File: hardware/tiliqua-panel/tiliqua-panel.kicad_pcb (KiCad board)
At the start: 2 copper layers, 30 x 128.5 mm, 13 parts

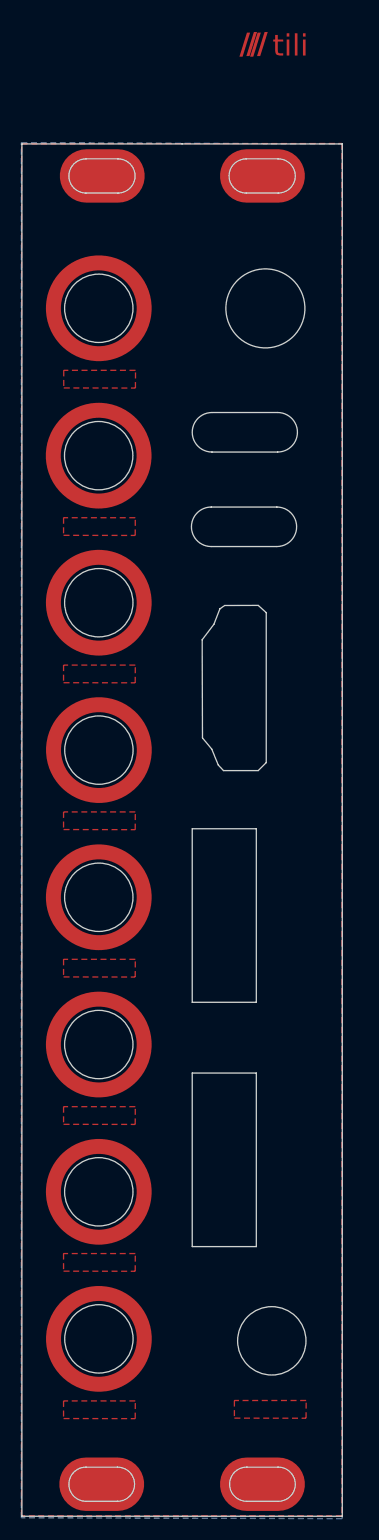
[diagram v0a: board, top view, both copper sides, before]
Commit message: fix panel slots and move some things
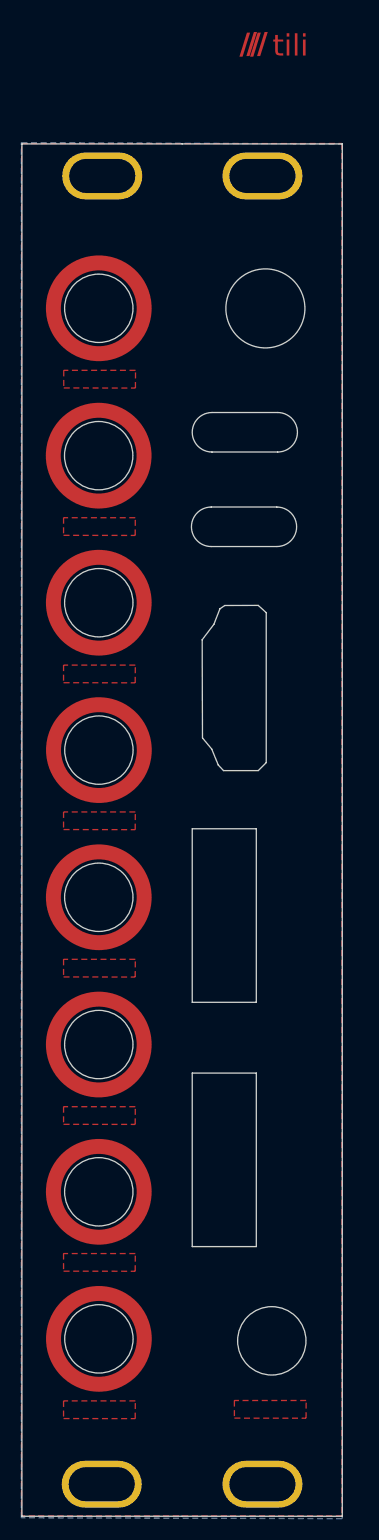
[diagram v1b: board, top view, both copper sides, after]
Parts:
- added E1: MountingHole_Pad, , F.Cu at (4.53, 3.00)
- added E2: MountingHole_Pad, , F.Cu at (19.5, 3.00)
- added E3: MountingHole_Pad, , F.Cu at (4.47, 125.5)
- added E4: MountingHole_Pad, , F.Cu at (19.5, 125.5)
- moved G*** 30.8 mm to (25.8, 72.0), turned to 0 degrees
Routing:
- added copper zone on B.Cu, net GND
- added copper zone on F.Cu, net GND
- removed copper zone on B.Cu, net (none)
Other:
- outline, holes or cut-outs redrawn
- board text added: "ctrl"
- board text added: "dbg"
- board text removed: "control"
- board text removed: "debug"

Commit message: more panel improvements
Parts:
- moved G*** 1.05 mm to (25.8, 73.1)
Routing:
- removed copper zone on F.Cu, net (none)
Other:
- board text added: "usb2"
- board text removed: "ctrl"
- board text removed: "usb"

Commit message: text top bottom looks good
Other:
- board text added: "[tiliqua]"
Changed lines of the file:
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@@
+	)
+	(gr_line
+		(start 17.4 7.5)
+		(end 25.9 7.5)
+		(stroke
+			(width 0.2)
+			(type default)
+		)
+		(layer "F.Mask")
 	)
 	(gr_line
@@
 		)
 		(fill solid)
+		(layer "F.Mask")
+	)
+	(gr_line
+		(start -1.8 7.5)
+		(end 6.9 7.5)
+		(stroke
+			(width 0.2)
+			(type default)
+		)
 		(layer "F.Mask")
 	)
@@
 				)
 			)
+		)
+	)
+	(gr_text "[tiliqua]"
+		(at 12.1 7.5 0)
+		(layer "F.Mask")
+		(effects
+			(font
+				(face "Space Grotesk")
+				(size 1.6 1.6)
+				(thickness 0.32)
+				(bold yes)
+			)
+		)
+		(render_cache "[tiliqua]" 0
+			(polygon
+				(pts
+					(xy 8.228849 8.715011) (xy 8.14766 8.702744) (xy 8.076276 8.662376) (xy 8.063936 8.650922) (xy 8.018215 8.583047)
+					(xy 8.000798 8.504978) (xy 8.000238 8.4864) (xy 8.000238 6.698933) (xy 8.01243 6.617819) (xy 8.052553 6.546681)
+					(xy 8.063936 6.534411) (xy 8.132091 6.48869) (xy 8.210267 6.471273) (xy 8.228849 6.470713) (xy 8.609477 6.470713)
+					(xy 8.609477 6.712611) (xy 8.333971 6.712611) (xy 8.27473 6.764073) (xy 8.27379 6.779826) (xy 8.27379 8.405898)
+					(xy 8.316634 8.471472) (xy 8.333971 8.473113) (xy 8.609477 8.473113) (xy 8.609477 8.715011)
+				)
+			)
+			(polygon
+				(pts
+					(xy 9.227705 8.164) (xy 9.145319 8.152713) (xy 9.071888 8.115313) (xy 9.049505 8.095612) (xy 9.003023 8.02702)
+					(xy 8.983168 7.947656) (xy 8.981508 7.913113) (xy 8.981508 7.285898) (xy 8.703657 7.285898) (xy 8.703657 7.052988)
+					(xy 8.981508 7.052988) (xy 8.981508 6.707921) (xy 9.263657 6.707921) (xy 9.263657 7.052988) (xy 9.568472 7.052988)
+					(xy 9.568472 7.285898) (xy 9.263657 7.285898) (xy 9.263657 7.863874) (xy 9.308449 7.929449) (xy 9.326574 7.93109)
+					(xy 9.541508 7.93109) (xy 9.541508 8.164)
+				)
+			)
+			(polygon
+				(pts
+					(xy 9.822876 8.164) (xy 9.822876 7.052988) (xy 10.105025 7.052988) (xy 10.105025 8.164)
+				)
+			)
+			(polygon
+				(pts
+					(xy 9.964341 6.922855) (xy 9.886031 6.907275) (xy 9.835381 6.873616) (xy 9.791331 6.804122) (xy 9.782624 6.743874)
+					(xy 9.799317 6.6632) (xy 9.835381 6.614132) (xy 9.906295 6.572693) (xy 9.964341 6.564502) (xy 10.04386 6.580205)
+					(xy 10.094083 6.614132) (xy 10.137153 6.683625) (xy 10.145667 6.743874) (xy 10.129345 6.824547)
+					(xy 10.094083 6.873616) (xy 10.023458 6.914729)
+				)
+			)
+			(polygon
+				(pts
+					(xy 10.418437 8.164) (xy 10.418437 6.596156) (xy 10.700587 6.596156) (xy 10.700587 8.164)
+				)
+			)
+			(polygon
+				(pts
+					(xy 11.013999 8.164) (xy 11.013999 7.052988) (xy 11.296148 7.052988) (xy 11.296148 8.164)
+				)
+			)
+			(polygon
+				(pts
+					(xy 11.155465 6.922855) (xy 11.077154 6.907275) (xy 11.026504 6.873616) (xy 10.982455 6.804122)
+					(xy 10.973748 6.743874) (xy 10.99044 6.6632) (xy 11.026504 6.614132) (xy 11.097419 6.572693) (xy 11.155465 6.564502)
+					(xy 11.234984 6.580205) (xy 11.285206 6.614132) (xy 11.328277 6.683625) (xy 11.33679 6.743874)
+					(xy 11.320469 6.824547) (xy 11.285206 6.873616) (xy 11.214582 6.914729)
+				)
+			)
+			(polygon
+				(pts
+					(xy 12.137555 7.025712) (xy 12.219423 7.041417) (xy 12.289142 7.072136) (xy 12.354779 7.122574)
+					(xy 12.404726 7.183379) (xy 12.40716 7.187419) (xy 12.447411 7.187419) (xy 12.447411 7.052988)
+					(xy 12.725262 7.052988) (xy 12.725262 8.611843) (xy 12.443113 8.611843) (xy 12.443113 8.036212)
+					(xy 12.402471 8.036212) (xy 12.352859 8.097671) (xy 12.3376 8.111634) (xy 12.270585 8.154125) (xy 12.226616 8.171815)
+					(xy 12.150412 8.189401) (xy 12.07027 8.195171) (xy 12.057795 8.195263) (xy 11.975722 8.188813)
+					(xy 11.897541 8.169464) (xy 11.823253 8.137217) (xy 11.808863 8.129219) (xy 11.741895 8.081951)
+					(xy 11.683627 8.022699) (xy 11.634061 7.951464) (xy 11.625192 7.935779) (xy 11.591756 7.859632)
+					(xy 11.569262 7.774954) (xy 11.558455 7.692522) (xy 11.556023 7.626274) (xy 11.556023 7.597356)
+					(xy 11.838172 7.597356) (xy 11.838172 7.619631) (xy 11.845065 7.704296) (xy 11.868894 7.78401)
+					(xy 11.914765 7.854242) (xy 11.925318 7.865046) (xy 11.990487 7.912882) (xy 12.065629 7.940861)
+					(xy 12.142596 7.949066) (xy 12.220853 7.940861) (xy 12.296445 7.912882) (xy 12.361047 7.865046)
+					(xy 12.410217 7.79814) (xy 12.437206 7.721447) (xy 12.447074 7.639503) (xy 12.447411 7.619631)
+					(xy 12.447411 7.597356) (xy 12.440487 7.512692) (xy 12.416551 7.432977) (xy 12.370475 7.362746)
+					(xy 12.359875 7.351941) (xy 12.294883 7.304106) (xy 12.219731 7.276126) (xy 12.142596 7.267921)
+					(xy 12.058386 7.277849) (xy 11.98415 7.307634) (xy 11.925318 7.351941) (xy 11.875703 7.418847)
+					(xy 11.84847 7.49554) (xy 11.838513 7.577484) (xy 11.838172 7.597356) (xy 11.556023 7.597356) (xy 11.556023 7.590713)
+					(xy 11.560346 7.503249) (xy 11.573315 7.422576) (xy 11.598241 7.339934) (xy 11.625192 7.281599)
+					(xy 11.667937 7.214602) (xy 11.723914 7.151618) (xy 11.788822 7.100694) (xy 11.810035 7.087768)
+					(xy 11.883766 7.05294) (xy 11.960855 7.031012) (xy 12.041303 7.021983) (xy 12.057795 7.021725)
+				)
+			)
+			(polygon
+				(pts
+					(xy 13.461899 8.181976) (xy 13.383733 8.176175) (xy 13.305068 8.156394) (xy 13.234069 8.122576)
+					(xy 13.167189 8.071596) (xy 13.112509 8.007757) (xy 13.082834 7.958054) (xy 13.052353 7.881866)
+					(xy 13.034524 7.798382) (xy 13.029296 7.716156) (xy 13.029296 7.052988) (xy 13.311836 7.052988)
+					(xy 13.311836 7.69349) (xy 13.319086 7.772344) (xy 13.346347 7.846484) (xy 13.37319 7.88185) (xy 13.442581 7.92673)
+					(xy 13.521335 7.943399) (xy 13.549044 7.944376) (xy 13.631584 7.934217) (xy 13.705828 7.899962)
+					(xy 13.750691 7.858403) (xy 13.791407 7.790946) (xy 13.813755 7.715597) (xy 13.821926 7.636363)
+					(xy 13.822206 7.617286) (xy 13.822206 7.052988) (xy 14.104746 7.052988) (xy 14.104746 8.164) (xy 13.826895 8.164)
+					(xy 13.826895 8.018235) (xy 13.786644 8.018235) (xy 13.738091 8.084234) (xy 13.68582 8.128438)
+					(xy 13.613233 8.163102) (xy 13.532167 8.17863)
+				)
+			)
+			(polygon
+				(pts
+					(xy 14.957623 7.025585) (xy 15.04173 7.039848) (xy 15.11701 7.06462) (xy 15.192237 7.105799) (xy 15.225527 7.131536)
+					(xy 15.281435 7.192426) (xy 15.321368 7.265674) (xy 15.345328 7.351281) (xy 15.35319 7.436326)
+					(xy 15.353315 7.449247) (xy 15.353315 7.863874) (xy 15.398107 7.929449) (xy 15.416232 7.93109)
+					(xy 15.505723 7.93109) (xy 15.505723 8.164) (xy 15.317753 8.164) (xy 15.237585 8.15264) (xy 15.180587 8.123748)
+					(xy 15.133375 8.059306) (xy 15.127049 8.016281) (xy 15.127049 8.013937) (xy 15.084453 8.013937)
+					(xy 15.044201 8.084669) (xy 14.984221 8.139696) (xy 14.945723 8.161655) (xy 14.866197 8.186861)
+					(xy 14.783455 8.194967) (xy 14.762052 8.195263) (xy 14.683286 8.190368) (xy 14.603996 8.173863)
+					(xy 14.549072 8.153839) (xy 14.479254 8.113926) (xy 14.418346 8.056951) (xy 14.400182 8.033085)
+					(xy 14.364759 7.962637) (xy 14.347395 7.880837) (xy 14.345471 7.839254) (xy 14.346331 7.830266)
+					(xy 14.627621 7.830266) (xy 14.651847 7.905831) (xy 14.674515 7.929136) (xy 14.750109 7.961711)
+					(xy 14.811291 7.967042) (xy 14.894236 7.957755) (xy 14.970202 7.926732) (xy 15.005123 7.900999)
+					(xy 15.056414 7.834641) (xy 15.078322 7.758288) (xy 15.080154 7.725144) (xy 15.080154 7.702478)
+					(xy 14.79566 7.702478) (xy 14.717927 7.713112) (xy 14.672171 7.736086) (xy 14.629753 7.805056)
+					(xy 14.627621 7.830266) (xy 14.346331 7.830266) (xy 14.353165 7.758837) (xy 14.378864 7.683378)
+					(xy 14.400182 7.647768) (xy 14.456474 7.587394) (xy 14.523212 7.54446) (xy 14.552589 7.531313)
+					(xy 14.629526 7.507261) (xy 14.707003 7.494965) (xy 14.775339 7.491843) (xy 15.080154 7.491843)
+					(xy 15.080154 7.429317) (xy 15.064574 7.349853) (xy 15.030915 7.300357) (xy 14.962164 7.261022)
+					(xy 14.880868 7.249994) (xy 14.874208 7.249945) (xy 14.792207 7.25922) (xy 14.720388 7.295422)
+					(xy 14.717111 7.298403) (xy 14.670455 7.361381) (xy 14.649896 7.422674) (xy 14.390021 7.335137)
+					(xy 14.422427 7.258532) (xy 14.465533 7.192923) (xy 14.476386 7.179603) (xy 14.536065 7.122948)
+					(xy 14.605278 7.079716) (xy 14.635437 7.065493) (xy 14.71633 7.038822) (xy 14.801296 7.025187)
+					(xy 14.878507 7.021725)
+				)
+			)
+			(polygon
+				(pts
+					(xy 15.590524 8.715011) (xy 15.590524 8.473113) (xy 15.86603 8.473113) (xy 15.925656 8.421651)
+					(xy 15.926602 8.405898) (xy 15.926602 6.779826) (xy 15.88348 6.714252) (xy 15.86603 6.712611) (xy 15.590524 6.712611)
+					(xy 15.590524 6.470713) (xy 15.971152 6.470713) (xy 16.052266 6.482905) (xy 16.123404 6.523028)
+					(xy 16.135674 6.534411) (xy 16.181675 6.602286) (xy 16.1992 6.680355) (xy 16.199763 6.698933) (xy 16.199763 8.4864)
+					(xy 16.187496 8.567515) (xy 16.147127 8.638652) (xy 16.135674 8.650922) (xy 16.067799 8.696924)
+					(xy 15.98973 8.714448) (xy 15.971152 8.715011)
+				)
+			)
